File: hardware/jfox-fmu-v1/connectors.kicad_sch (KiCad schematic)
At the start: 11 parts, among them J1 TELEM1, J10 SAFETY, J11 PWM_OUT, J2 TELEM2, J3 GPS1, J4 GPS2, J5 RC_IN, J6 DEBUG, J7 SPI_EXT, J8 PWR_BRICK, J9 PWR_SERVO

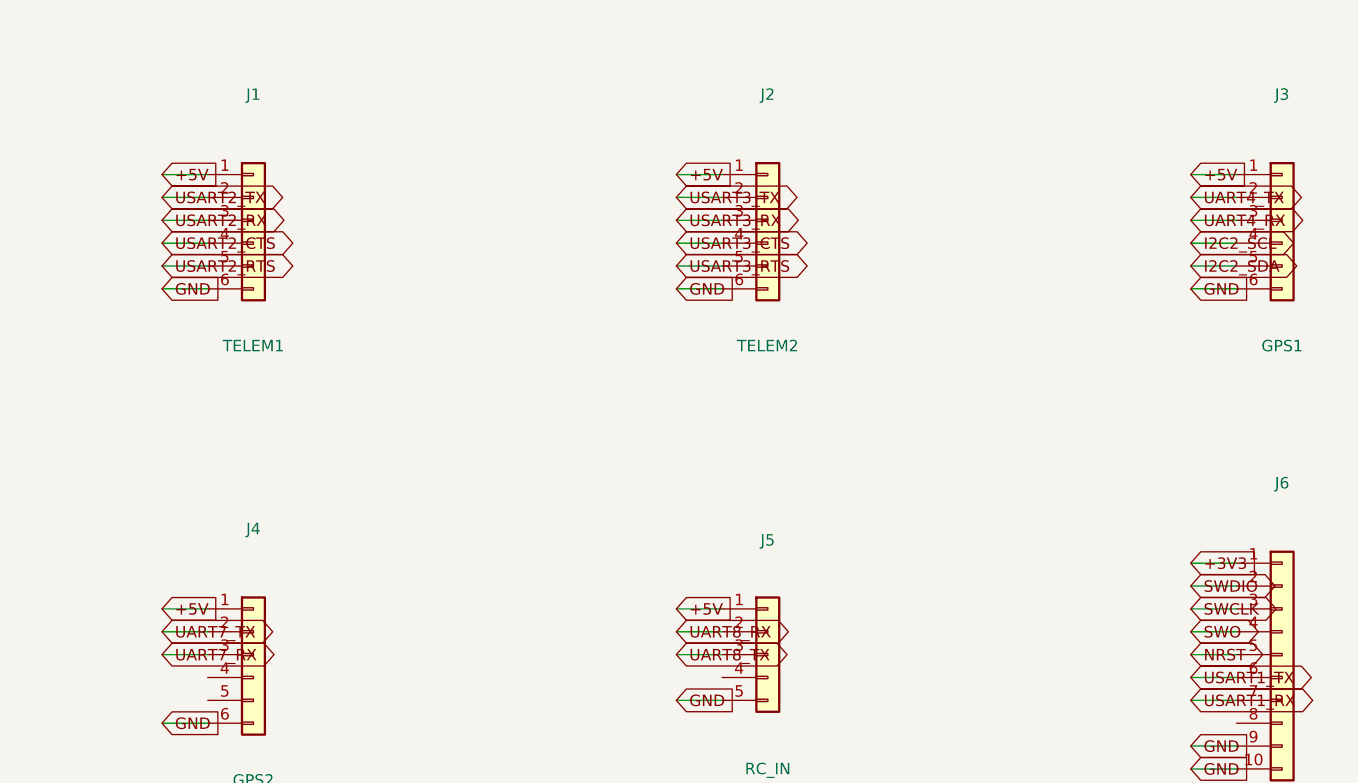
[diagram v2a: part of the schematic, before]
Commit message: EMI/EMC protection, and the stackup that actually decides it
Full review first: schematic, footprints, sheet fit and traceability all pass;
objective passes 12 of 13 with fibre the only gap; environmental passes the
category and reports its known gaps. ERC 89, of which 75 are deliberately
unallocated GPIO.

A new protection sheet closes HWR-ENV-006 and HWR-ENV-007, and adds the
emissions control that DO-160G s21 would otherwise fail on. This board carries
two deliberate switching sources - U21 at 2.5 MHz and each ISOW1044's internal
converter at 25 MHz - and every off-board harness is an antenna bonded to
them.

  D4/D5/D6  6 V TVS on brick, servo and USB inputs. Above the 5.5 V a valid
            supply reaches, below what the LTC4417 and the buck tolerate.
            Unidirectional - reverse battery is the LTC4417's job.
  U40       USBLC6-2SC6 between J30 and the choke, closest to the connector
            so it protects the choke too, not only the MCU.
  L5        common-mode choke on USB, after the ESD array.
  L3/L4     common-mode chokes on both CAN pairs, with D7/D8 across them.
  FB1-3     ferrites on the 5 V feed to the telemetry, GPS and RC harnesses,
            because conducted emissions leave on the power wire as readily as
            on the signal wires.

The CAN protection references GND_ISO, not GND. Referencing it to board ground
would bridge the isolation barrier and undo the reason the ISOW1044 is there.

PCB_STACKUP_AND_EMC.md carries the half of EMC that is not a component:

**Six layers, not four.** A 4-layer SIG/GND/PWR/SIG leaves the inner power
layer split - and this board splits it four ways for the switched sensor rails
plus the analog and isolated domains. A signal crossing a split has no return
beneath it, so the return detours and the loop it encloses is the radiating
element. Six layers puts solid ground either side of the power layer, so every
signal has an unbroken return whatever the power layer is doing. That is the
single mos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
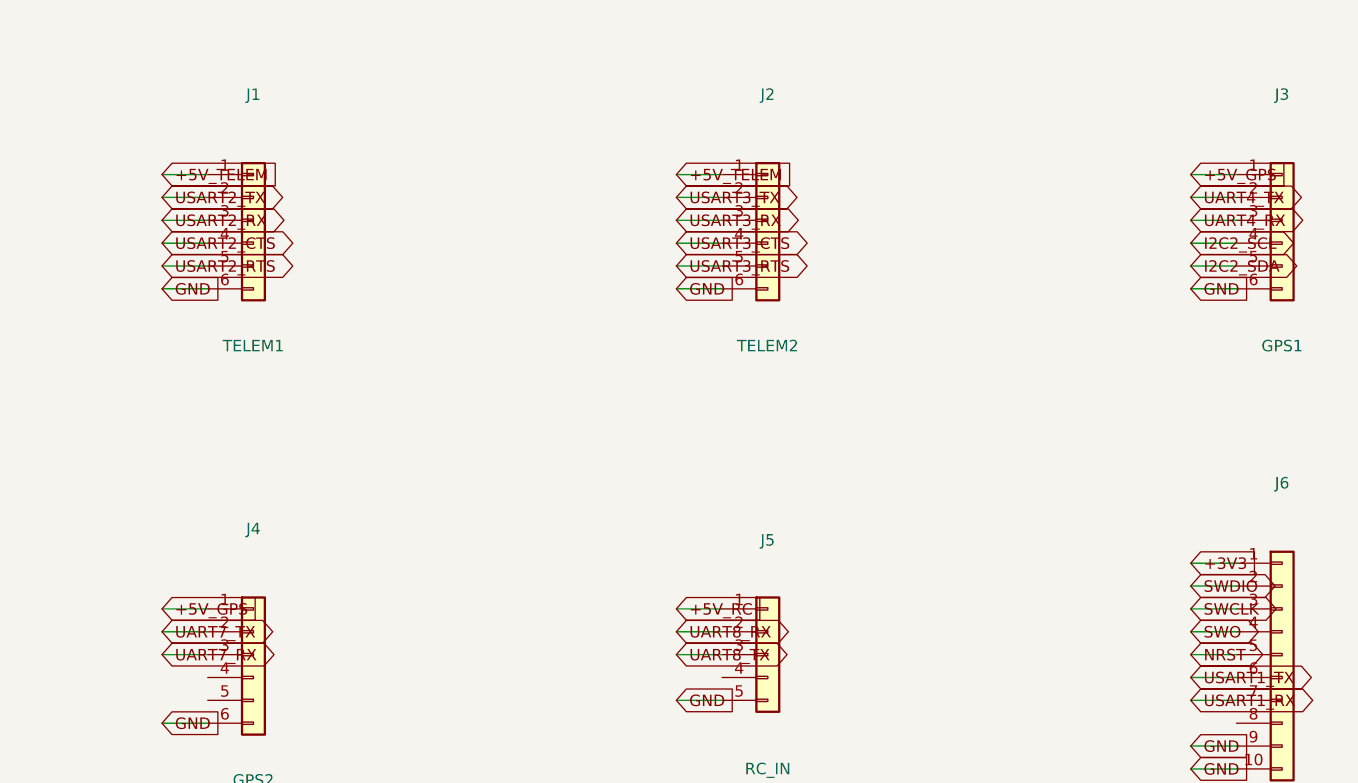
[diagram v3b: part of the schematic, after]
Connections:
- removed net +5V: J1.1 (Pin_1), J2.1 (Pin_1), J3.1 (Pin_1), J4.1 (Pin_1), J5.1 (Pin_1)
- new net +5V_GPS: J3.1 (Pin_1), J4.1 (Pin_1)
- new net +5V_RC: J5.1 (Pin_1)
- new net +5V_TELEM: J1.1 (Pin_1), J2.1 (Pin_1)
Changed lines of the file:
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@@
 		(instances
 			(project "jfox-fmu"
-				(path "/c24b2d08-5c44-4721-9853-c5ca3d469d4d"
+				(path "/097ca2d3-06b6-4e75-8745-771336e2c876"
 					(reference "J1")
 					(unit 1)
@@
 		)
 	)
-	(global_label "+5V"
+	(global_label "+5V_TELEM"
 		(shape input)
 		(at 54.61 59.69 0)
@@
 		(instances
 			(project "jfox-fmu"
-				(path "/c24b2d08-5c44-4721-9853-c5ca3d469d4d"
+				(path "/097ca2d3-06b6-4e75-8745-771336e2c876"
 					(reference "J2")
 					(unit 1)
@@
 		)
 	)
-	(global_label "+5V"
+	(global_label "+5V_TELEM"
 		(shape input)
 		(at 111.76 59.69 0)
@@
 		(instances
 			(project "jfox-fmu"
-				(path "/c24b2d08-5c44-4721-9853-c5ca3d469d4d"
+				(path "/097ca2d3-06b6-4e75-8745-771336e2c876"
 					(reference "J3")
 					(unit 1)
@@
 		)
 	)
-	(global_label "+5V"
+	(global_label "+5V_GPS"
 		(shape input)
 		(at 168.91 59.69 0)
@@
 		(instances
 			(project "jfox-fmu"
-				(path "/c24b2d08-5c44-4721-9853-c5ca3d469d4d"
+				(path "/097ca2d3-06b6-4e75-8745-771336e2c876"
 					(reference "J4")
 					(unit 1)
@@
 		)
 	)
-	(global_label "+5V"
+	(global_label "+5V_GPS"
 		(shape input)
 		(at 54.61 107.95 0)
@@
 		(instances
 			(project "jfox-fmu"
-				(path "/c24b2d08-5c44-4721-9853-c5ca3d469d4d"
+				(path "/097ca2d3-06b6-4e75-8745-771336e2c876"
 					(reference "J5")
 					(unit 1)
@@
 		)
 	)
-	(global_label "+5V"
+	(global_label "+5V_RC"
 		(shape input)
 		(at 111.76 107.95 0)
@@
 		(instances
 			(project "jfox-fmu"
-				(path "/c24b2d08-5c44-4721-9853-c5ca3d469d4d"
+				(path "/097ca2d3-06b6-4e75-8745-771336e2c876"
 					(reference "J6")
 					(unit 1)
@@
 		(instances
 			(project "jfox-fmu"
-				(path "/c24b2d08-5c44-4721-9853-c5ca3d469d4d"
+				(path "/097ca2d3-06b6-4e75-8745-771336e2c876"
 					(reference "J7")
 					(unit 1)
@@
 		(instances
 			(project "jfox-fmu"
-				(path "/c24b2d08-5c44-4721-9853-c5ca3d469d4d"
+				(path "/097ca2d3-06b6-4e75-8745-771336e2c876"
 					(reference "J8")
 					(unit 1)
@@
 		(instances
 			(project "jfox-fmu"
-				(path "/c24b2d08-5c44-4721-9853-c5ca3d469d4d"
+				(path "/097ca2d3-06b6-4e75-8745-771336e2c876"
 					(reference "J9")
 					(unit 1)
@@
 		(instances
 			(project "jfox-fmu"
-				(path "/c24b2d08-5c44-4721-9853-c5ca3d469d4d"
+				(path "/097ca2d3-06b6-4e75-8745-771336e2c876"
 					(reference "J10")
 					(unit 1)
@@
 		(instances
 			(project "jfox-fmu"
-				(path "/c24b2d08-5c44-4721-9853-c5ca3d469d4d"
+				(path "/097ca2d3-06b6-4e75-8745-771336e2c876"
 					(reference "J11")
 					(unit 1)

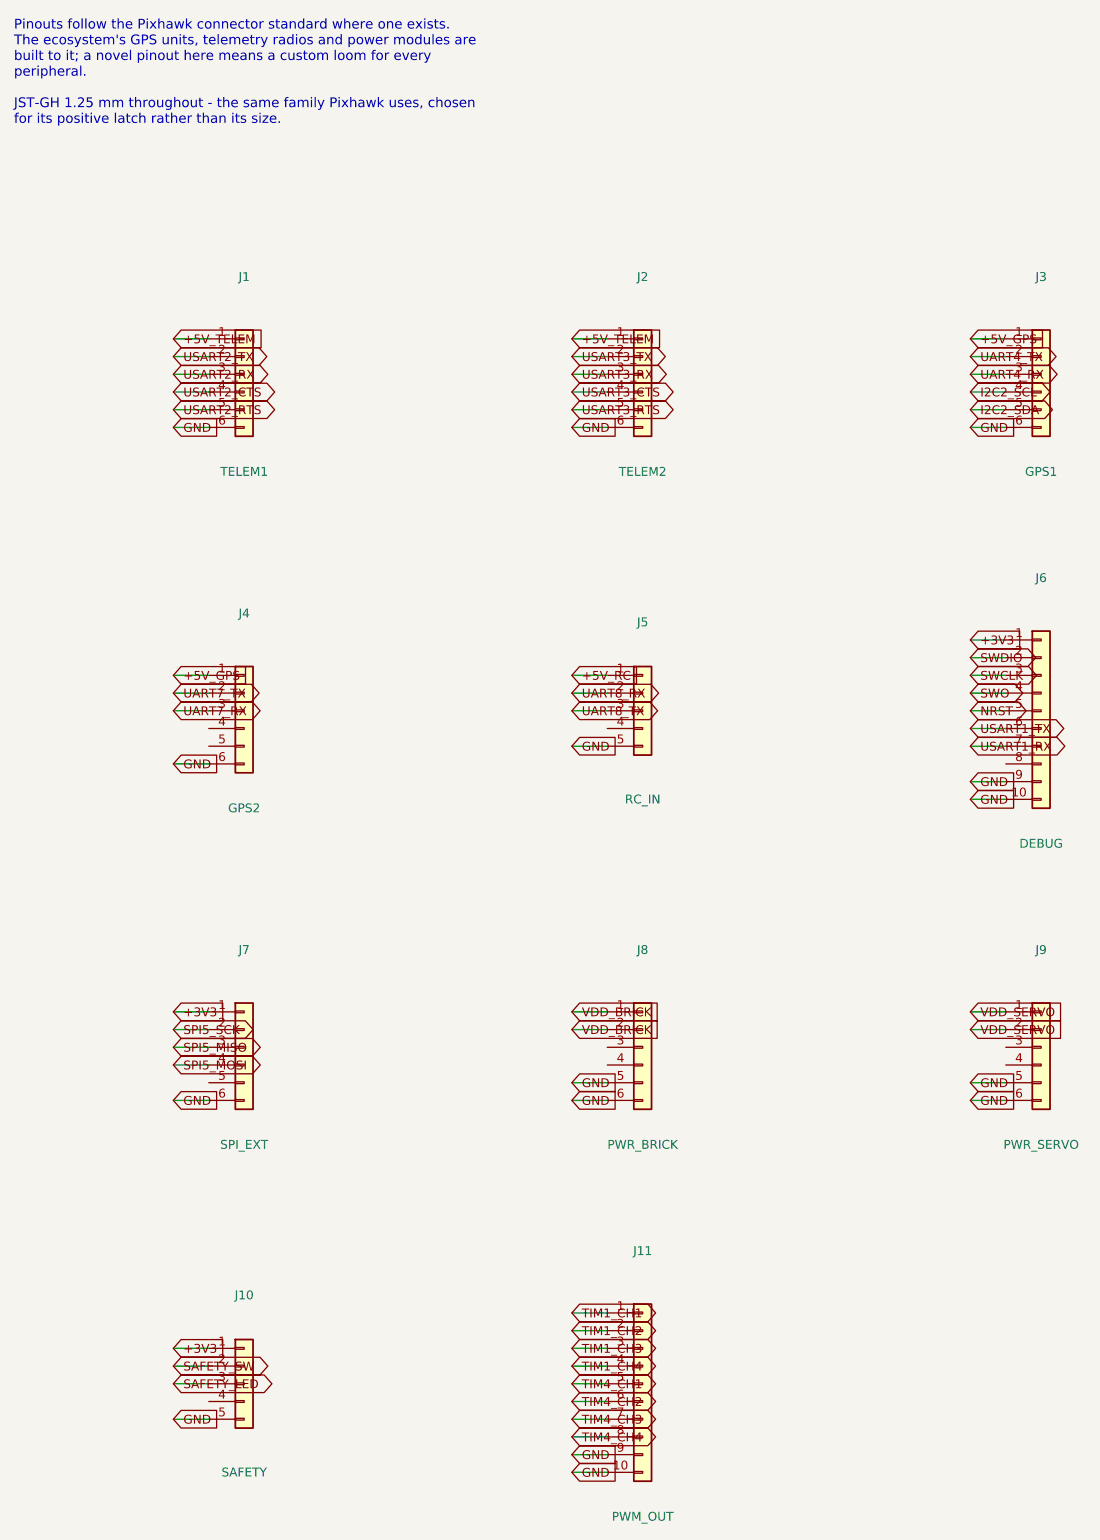
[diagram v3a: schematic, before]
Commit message: Mezzanine to the carrier, microSD on the edge, sensors moved clear
Three placement changes, and the third is now measured rather than asserted.

QUICK ASSEMBLY. Ten JST-GH headers become one 60-way 0.5 mm mezzanine
(DF12C3.0-60DS) to the carrier, which is what ARCHITECTURE.md already argued
for: eleven looms is eleven things to make, inspect and vibrate loose.
Grounds are interleaved between signal groups rather than grouped at one end,
because a 60-pin connector with no local return is the worst discontinuity on
a board.

What deliberately does NOT cross it: the isolated CAN. A 0.5 mm pitch gives
about 0.5 mm of creepage between adjacent contacts, so running CAN1_H/L
alongside board-referenced signals would quietly reduce the isolation barrier
to that gap - which defeats the ISOW1044 entirely. CAN keeps dedicated
connectors on the isolated side. Debug, USB and the card slot also stay on the
module, because they are used at the module: putting them on the carrier means
unbolting the aircraft to read a log.

The three ferrites became one. Every harness now leaves through the mezzanine,
so there is one 5 V feed to filter instead of three - and three ferrites
driving nets nothing connects to is worse than none.

MICROSD ON THE EDGE, aligned by COURTYARD rather than origin. The first
attempt placed it by its origin and hung a 15 mm deep socket off the board.
The card now ejects outward, off the board, not into U10.

SENSORS MOVED, and the reason checked. The mezzanine freed ten headers' worth
of edge, so the sensors get a dedicated island in the bottom-left - the corner
furthest from both the buck at top-left and the isolated converters at
top-right. The magnetometer is placed by hand in the far corner rather than
packed, because DO-160G s15 makes it the most placement-sensitive part here.

check_fmu_placement.py measures it. "Keep the sensors away from the noise" is
obviously right, impossible to argue with, and untestable as written. Each
sensitive part now has a mini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
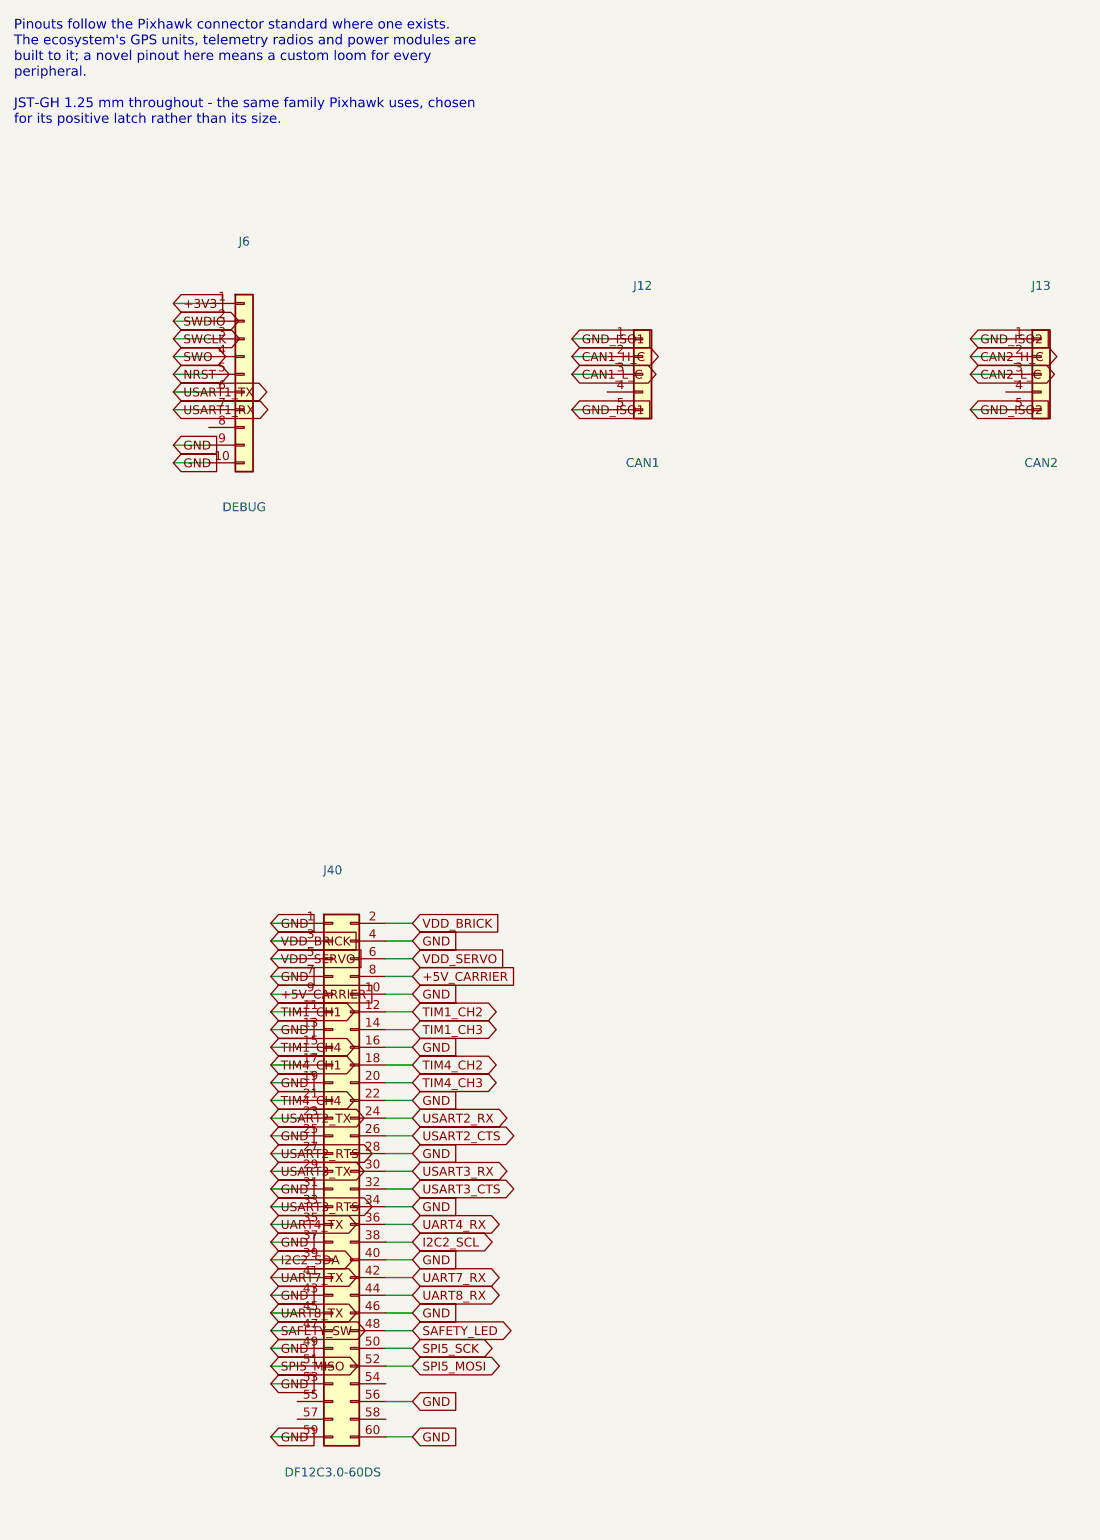
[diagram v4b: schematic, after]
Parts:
- removed J1: TELEM1, Connector_JST:JST_GH_SM06B-GHS-TB_1x06-1MP_P1.25mm_Horizontal, symbol Connector_Generic:Conn_01x06
- removed J10: SAFETY, Connector_JST:JST_GH_SM05B-GHS-TB_1x05-1MP_P1.25mm_Horizontal, symbol Connector_Generic:Conn_01x05
- removed J11: PWM_OUT, Connector_JST:JST_GH_SM10B-GHS-TB_1x10-1MP_P1.25mm_Horizontal, symbol Connector_Generic:Conn_01x10
- removed J2: TELEM2, Connector_JST:JST_GH_SM06B-GHS-TB_1x06-1MP_P1.25mm_Horizontal, symbol Connector_Generic:Conn_01x06
- removed J3: GPS1, Connector_JST:JST_GH_SM06B-GHS-TB_1x06-1MP_P1.25mm_Horizontal, symbol Connector_Generic:Conn_01x06
- removed J4: GPS2, Connector_JST:JST_GH_SM06B-GHS-TB_1x06-1MP_P1.25mm_Horizontal, symbol Connector_Generic:Conn_01x06
- removed J5: RC_IN, Connector_JST:JST_GH_SM05B-GHS-TB_1x05-1MP_P1.25mm_Horizontal, symbol Connector_Generic:Conn_01x05
- removed J7: SPI_EXT, Connector_JST:JST_GH_SM06B-GHS-TB_1x06-1MP_P1.25mm_Horizontal, symbol Connector_Generic:Conn_01x06
- removed J8: PWR_BRICK, Connector_JST:JST_GH_SM06B-GHS-TB_1x06-1MP_P1.25mm_Horizontal, symbol Connector_Generic:Conn_01x06
- removed J9: PWR_SERVO, Connector_JST:JST_GH_SM06B-GHS-TB_1x06-1MP_P1.25mm_Horizontal, symbol Connector_Generic:Conn_01x06
- added J12: CAN1, Connector_JST:JST_GH_SM05B-GHS-TB_1x05-1MP_P1.25mm_Horizontal, symbol Connector_Generic:Conn_01x05
- added J13: CAN2, Connector_JST:JST_GH_SM05B-GHS-TB_1x05-1MP_P1.25mm_Horizontal, symbol Connector_Generic:Conn_01x05
- added J40: DF12C3.0-60DS, Connector_Hirose:Hirose_DF12_DF12C3.0-60DS-0.5V_2x30_P0.50mm_Vertical, symbol Connector_Generic:Conn_02x30_Odd_Even
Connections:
- net GND: now also J40.1 (Pin_1), J40.10 (Pin_10), J40.13 (Pin_13), J40.16 (Pin_16), J40.19 (Pin_19), J40.22 (Pin_22), J40.25 (Pin_25), J40.28 (Pin_28), J40.31 (Pin_31), J40.34 (Pin_34), J40.37 (Pin_37), J40.4 (Pin_4), J40.40 (Pin_40), J40.43 (Pin_43), J40.46 (Pin_46), J40.49 (Pin_49), J40.53 (Pin_53), J40.56 (Pin_56), J40.59 (Pin_59), J40.60 (Pin_60), J40.7 (Pin_7)
- net I2C2_SCL: now also J40.38 (Pin_38)
- net I2C2_SDA: now also J40.39 (Pin_39)
- net SAFETY_LED: now also J40.48 (Pin_48)
- net SAFETY_SW: now also J40.47 (Pin_47)
- net SPI5_MISO: now also J40.51 (Pin_51)
- net SPI5_MOSI: now also J40.52 (Pin_52)
- net SPI5_SCK: now also J40.50 (Pin_50)
- net TIM1_CH1: now also J40.11 (Pin_11)
- net TIM1_CH2: now also J40.12 (Pin_12)
- net TIM1_CH3: now also J40.14 (Pin_14)
- net TIM1_CH4: now also J40.15 (Pin_15)
- net TIM4_CH1: now also J40.17 (Pin_17)
- net TIM4_CH2: now also J40.18 (Pin_18)
- net TIM4_CH3: now also J40.20 (Pin_20)
- net TIM4_CH4: now also J40.21 (Pin_21)
- net UART4_RX: now also J40.36 (Pin_36)
- net UART4_TX: now also J40.35 (Pin_35)
- net UART7_RX: now also J40.42 (Pin_42)
- net UART7_TX: now also J40.41 (Pin_41)
- net UART8_RX: now also J40.44 (Pin_44)
- net UART8_TX: now also J40.45 (Pin_45)
- net USART2_CTS: now also J40.26 (Pin_26)
- net USART2_RTS: now also J40.27 (Pin_27)
- net USART2_RX: now also J40.24 (Pin_24)
- net USART2_TX: now also J40.23 (Pin_23)
- net USART3_CTS: now also J40.32 (Pin_32)
- net USART3_RTS: now also J40.33 (Pin_33)
- net USART3_RX: now also J40.30 (Pin_30)
- net USART3_TX: now also J40.29 (Pin_29)
- net VDD_BRICK: now also J40.2 (Pin_2), J40.3 (Pin_3)
- net VDD_SERVO: now also J40.5 (Pin_5), J40.6 (Pin_6)
- new net +5V_CARRIER: J40.8 (Pin_8), J40.9 (Pin_9)
- new net CAN1_H_C: J12.2 (Pin_2)
- new net CAN1_L_C: J12.3 (Pin_3)
- new net CAN2_H_C: J13.2 (Pin_2)
- new net CAN2_L_C: J13.3 (Pin_3)
- new net GND_ISO1: J12.1 (Pin_1), J12.5 (Pin_5)
- new net GND_ISO2: J13.1 (Pin_1), J13.5 (Pin_5)
